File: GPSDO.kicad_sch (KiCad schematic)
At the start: 86 parts, among them J1 Conn_Coaxial, J10 PROG, J2 GPS_CONN, J3 Conn_Coaxial, J4 Conn_Coaxial, J5 Conn_Coaxial, J6 Conn_Coaxial, J7 DISP_MODULE, J8 Barrel_Jack, SW1 RESET_BTN, U1 REF3450, U10 MC7805BDTRKG, U11 74AUC1G74, U12 74AUC2G04, U13 74AUC2G04, U14 DS34C87T, U2 74LVC1G125SE-7, U3 AD5680, U4 NB3N551MN, U5 LTC2050IS8, U6 AVR32DB28x-xSO, U7 74LVC1G125SE-7, U8 74HC390, U9 L7805CV, X1 OC5SC25

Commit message: minor adjustments
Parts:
- added D1: LED, LED_SMD:LED_0805_2012Metric, symbol Device:LED
- added R5: 270R, Resistor_SMD:R_0805_2012Metric_Pad1.20x1.40mm_HandSolder, symbol Device:R_Small_US
- H1, H2, H3, H4: footprint MountingHole:MountingHole_3.2mm_M3_Pad -> MountingHole:MountingHole_4.3mm_M4_Pad
- U9: footprint Package_TO_SOT_THT:TO-220-3_Horizontal_TabDown -> Package_TO_SOT_THT:TO-220-3_Vertical
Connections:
- net DIV_RESET is gone; now on net TOUCH_IRQ: U6.8 (PD2)
- net +5VA: no longer C1.1
- net +5VD: now also C1.1
- net GND: now also C1.2, R5.1
- net GNDA: no longer C1.2
- net TOUCH_IRQ: no longer U6.11 (PD5)
- net at U6.10 (PD4): now also D1.2 (A)
- new net: D1.1 (K), R5.2

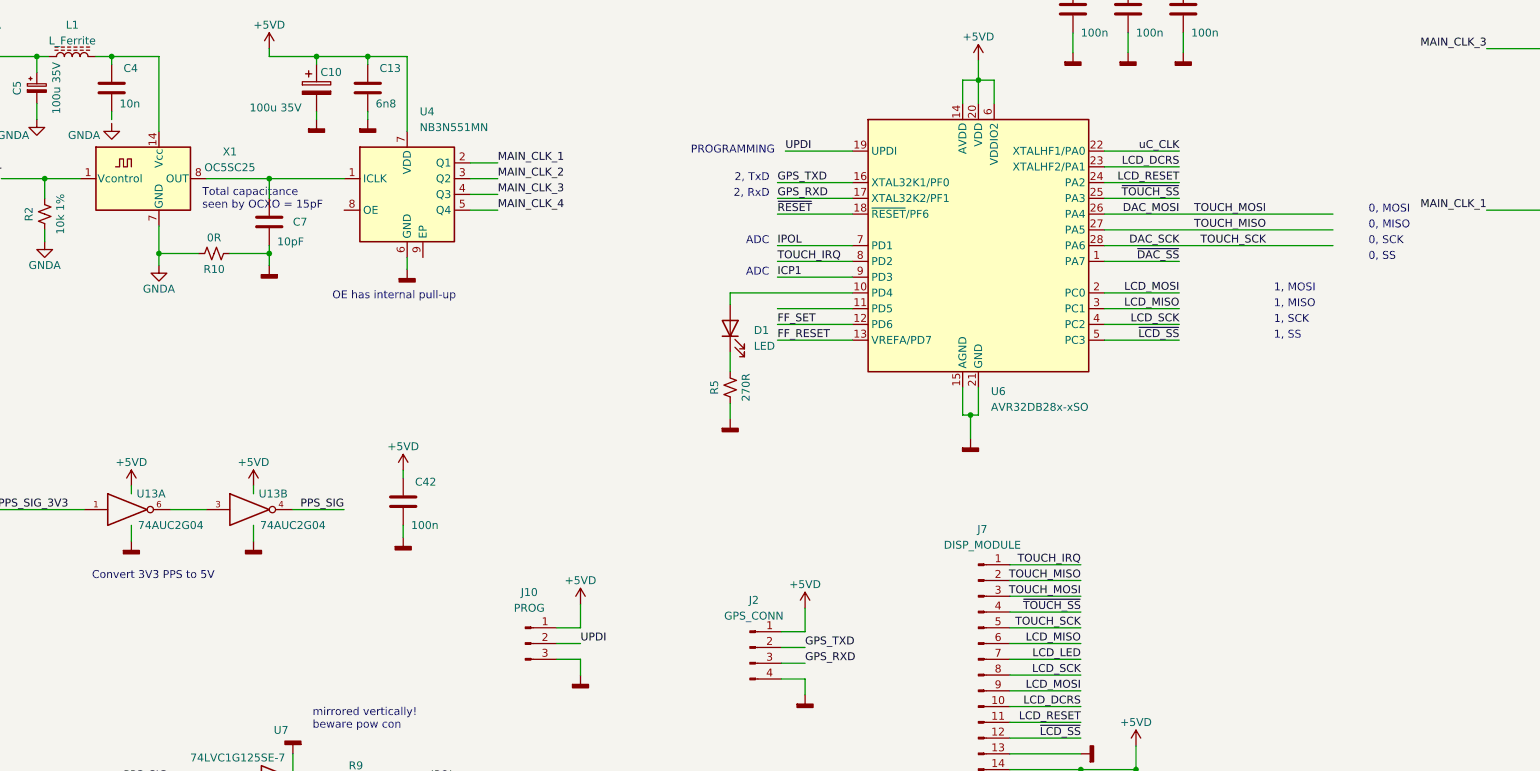
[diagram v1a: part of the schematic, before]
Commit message: Re-assigned pins
Preparing for tracing
Added an UFL output for an arbitrary clock out from the uC. Undecided on PCB dimensions ... will probably change from line driver to RS422 driver and go for a wider PCB
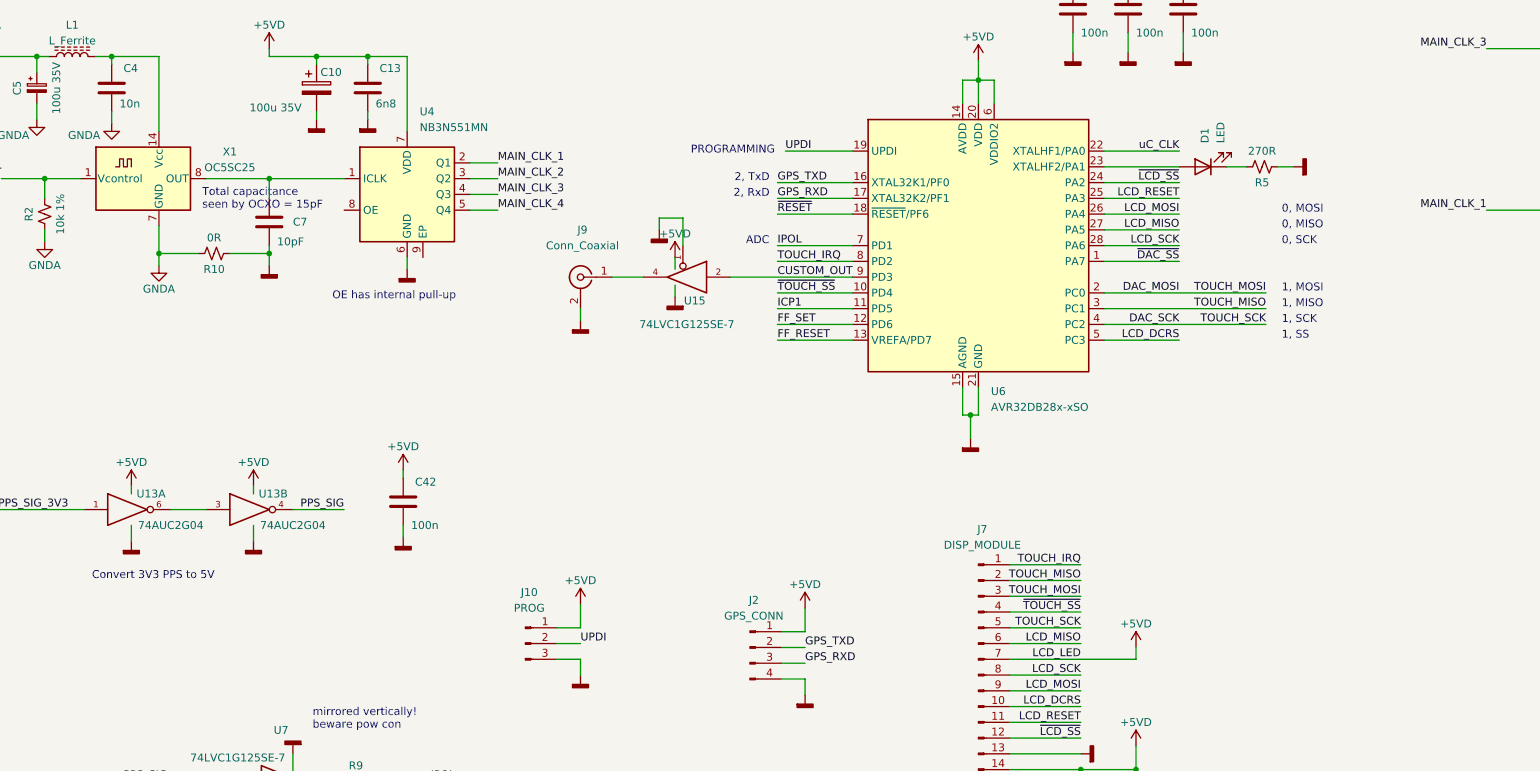
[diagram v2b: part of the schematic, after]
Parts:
- added J9: Conn_Coaxial, Connector_Coaxial:U.FL_Molex_MCRF_73412-0110_Vertical, symbol Connector:Conn_Coaxial
- added U15: 74LVC1G125SE-7, Package_TO_SOT_SMD:SOT-353_SC-70-5, symbol 74xGxx:74AUC1G125
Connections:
- net LCD_LED is gone; now on net +5VD: J7.7 (Pin_7)
- net +5VD: now also U15.5 (VCC)
- net DAC_MOSI: now also U6.2 (PC0); no longer U6.26 (PA4)
- net DAC_SCK: now also U6.4 (PC2); no longer U6.28 (PA6)
- net GND: now also J9.2 (Ext), U15.1, U15.3 (GND)
- net GNDA: now also C4.1
- net ICP1: now also U6.11 (PD5); no longer U6.9 (PD3)
- net LCD_DCRS: now also U6.5 (PC3); no longer U6.23 (XTALHF2/PA1)
- net LCD_MISO: now also U6.27 (PA5); no longer U6.3 (PC1)
- net LCD_MOSI: now also U6.26 (PA4); no longer U6.2 (PC0)
- net LCD_RESET: now also U6.25 (PA3); no longer U6.24 (PA2)
- net LCD_SCK: now also U6.28 (PA6); no longer U6.4 (PC2)
- net TOUCH_MISO: now also U6.3 (PC1); no longer U6.27 (PA5)
- net ~{LCD_SS}: now also U6.24 (PA2); no longer U6.5 (PC3)
- net ~{TOUCH_SS}: now also U6.10 (PD4); no longer U6.25 (PA3)
- net at D1.2 (A): now also U6.23 (XTALHF2/PA1); no longer U6.10 (PD4)
- new net: J9.1 (In), U15.4
- new net CUSTOM_OUT: U15.2, U6.9 (PD3)
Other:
- note removed: "0, SS"
- moved on the sheet: D1, R5

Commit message: updated pcb
more shuffling
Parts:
- added C46: 100n, Capacitor_SMD:C_0805_2012Metric_Pad1.18x1.45mm_HandSolder, symbol Device:C
- H1, H2, H3, H4: footprint MountingHole:MountingHole_4.3mm_M4_Pad -> MountingHole:MountingHole_3.2mm_M3_Pad_Via
- X1: footprint Oscillator:Oscillator_DIP-14 -> custom:OC5SC25
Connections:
- net +5VD: now also C46.2
- net 1Mc_CLK: now also U14.1 (INPUT); no longer U14.7 (INPUT)
- net CUSTOM_OUT: now also U6.10 (PD4); no longer U6.9 (PD3)
- net GND: now also C46.1
- net LCD_DCRS: now also U6.25 (PA3); no longer U6.5 (PC3)
- net LCD_RESET: now also U6.24 (PA2); no longer U6.25 (PA3)
- net MAIN_CLK_3: now also U14.7 (INPUT); no longer U14.1 (INPUT)
- net ~{LCD_SS}: now also U6.23 (XTALHF2/PA1); no longer U6.24 (PA2)
- net ~{TOUCH_SS}: now also U6.5 (PC3); no longer U6.10 (PD4)
- net at C29.2: now also J5.1 (In); no longer J3.1 (In)
- net at U14.13 (OUT-): now also C39.1; no longer C38.1
- net at U14.14 (OUT+): now also C38.1; no longer C39.1
- net at C30.2: now also J5.2 (Ext); no longer J3.2 (Ext)
- net at D1.2 (A): now also U6.9 (PD3); no longer U6.23 (XTALHF2/PA1)
- net at U14.2 (OUT+): now also C40.1; no longer C41.1
- net at U14.3 (OUT-): now also C41.1; no longer C40.1
- net at C41.2: now also J3.2 (Ext); no longer J5.2 (Ext)
- net at C40.2: now also J3.1 (In); no longer J5.1 (In)
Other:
- moved on the sheet: C29, C30, C38, C39, C40, C41, D1, J3, J6, J9, R4, R5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

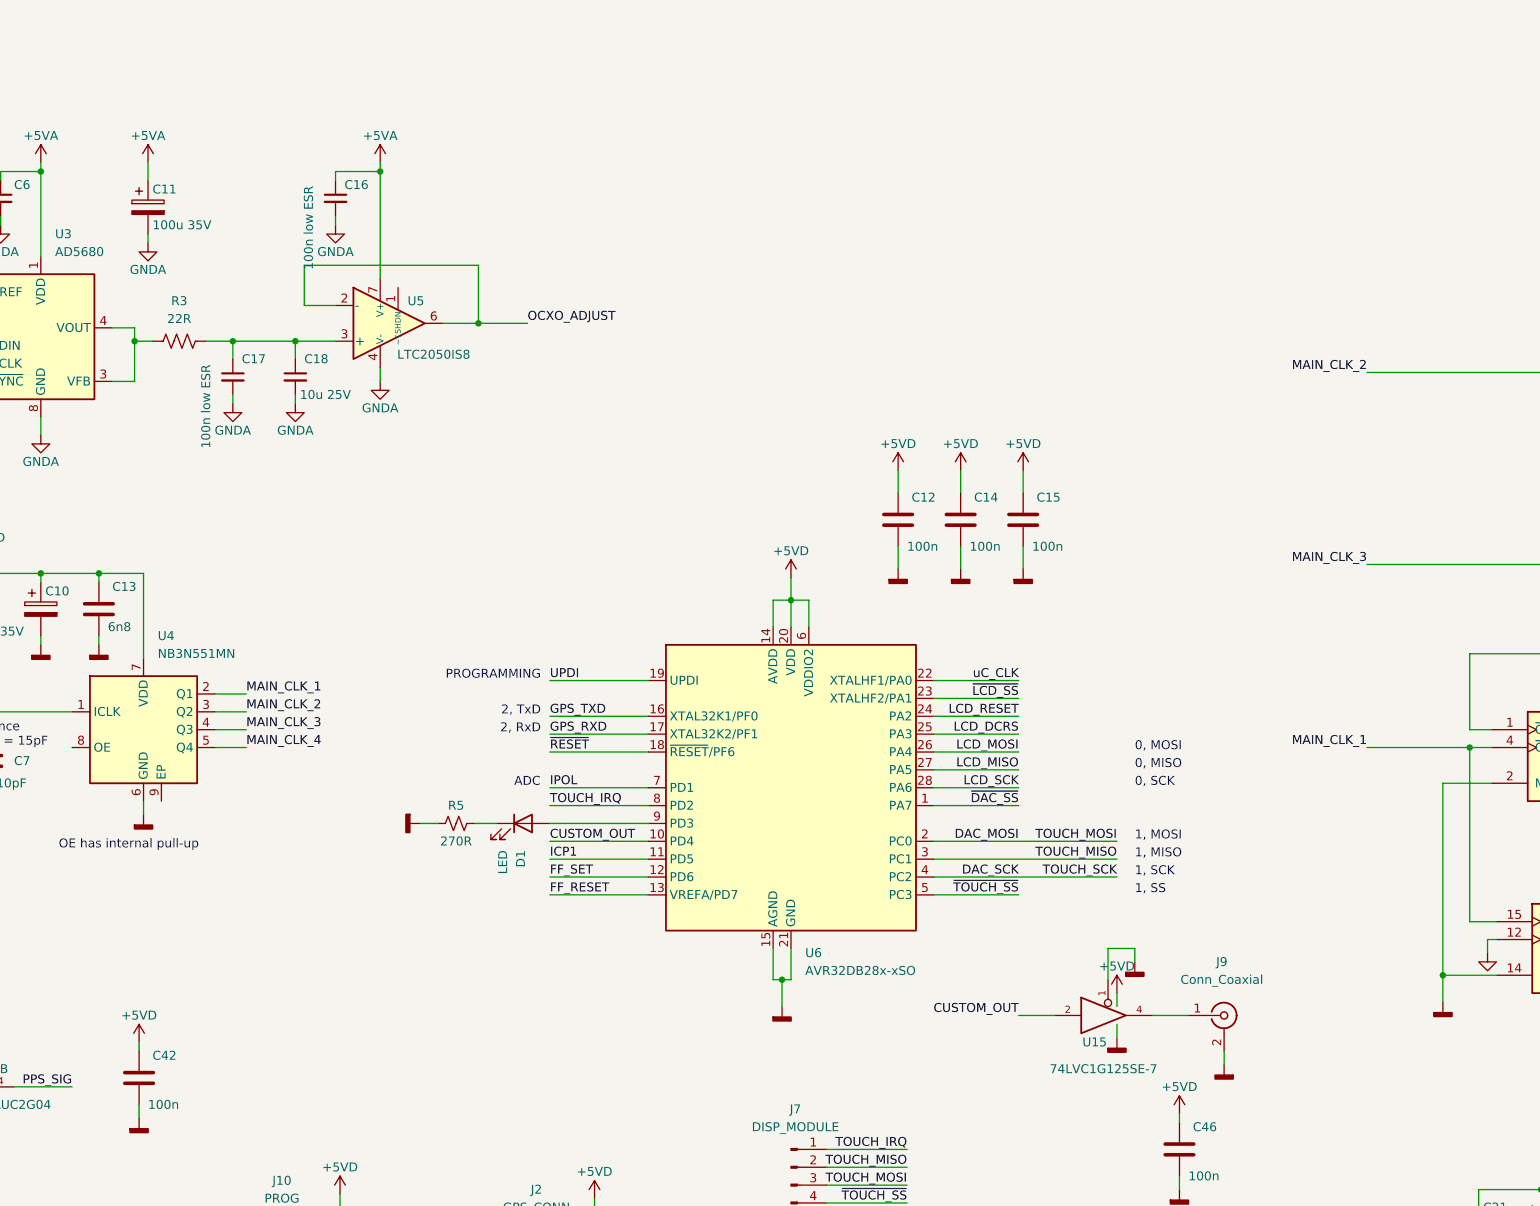
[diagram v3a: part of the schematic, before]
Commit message: component placement
inching towards completion
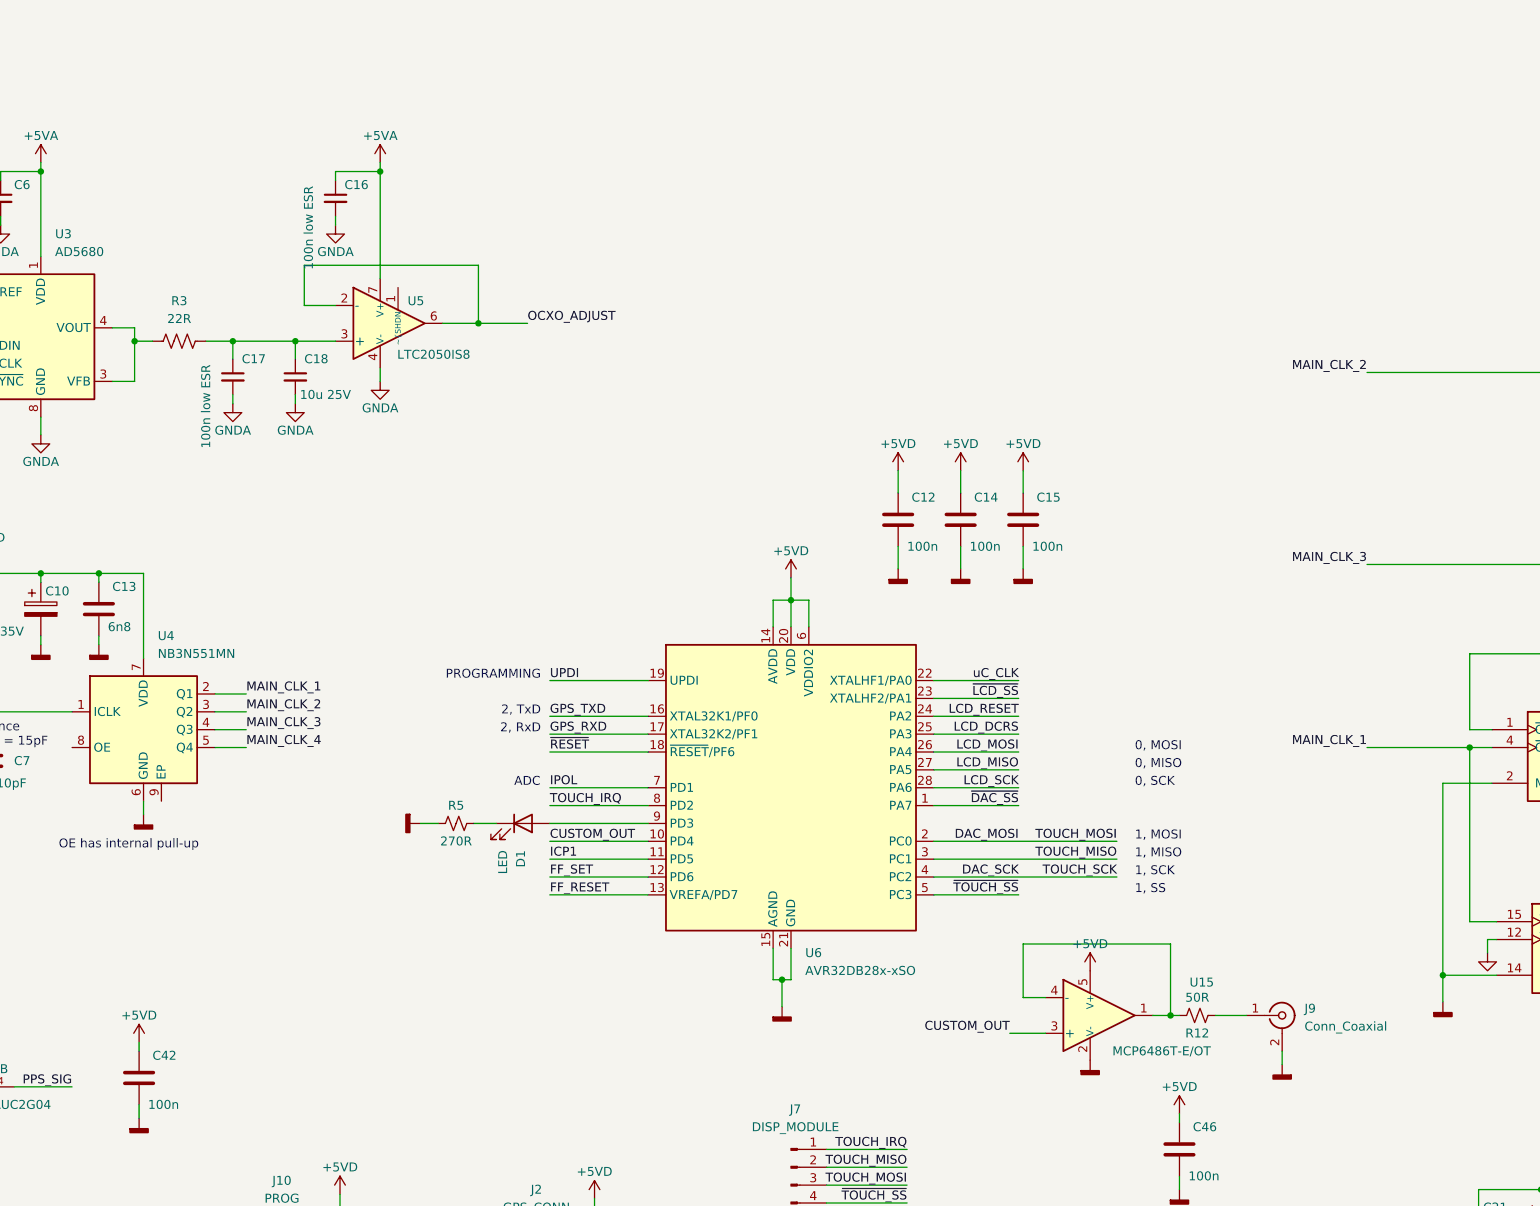
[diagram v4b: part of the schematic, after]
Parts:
- removed C11: 100u 35V, Capacitor_SMD:C_Elec_6.3x7.7, symbol Device:C_Polarized
- removed U15: 74LVC1G125SE-7, Package_TO_SOT_SMD:SOT-353_SC-70-5, symbol 74xGxx:74AUC1G125
- added R12: 50R, Resistor_SMD:R_0805_2012Metric_Pad1.20x1.40mm_HandSolder, symbol Device:R_Small_US
- added U15: MCP6486T-E/OT, Package_TO_SOT_SMD:SOT-23-5_HandSoldering, symbol Amplifier_Operational_AKL:MCP6481T-E-LTY
- J9: footprint Connector_Coaxial:U.FL_Molex_MCRF_73412-0110_Vertical -> Connector_Coaxial:SMA_Amphenol_901-143_Horizontal
- U9: footprint Package_TO_SOT_THT:TO-220-3_Vertical -> Package_TO_SOT_THT:TO-220-3_Horizontal_TabDown
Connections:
- net +5VD: now also U15.5 (V+)
- net CUSTOM_OUT: now also U15.3 (+)
- net GND: now also U15.2 (V-)
- net at J9.1 (In): now also R12.1
- new net: R12.2, U15.1, U15.4 (-)
